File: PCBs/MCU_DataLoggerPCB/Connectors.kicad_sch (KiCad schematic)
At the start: 4 parts, among them J1 Conn_01x04_Pin, J2 Conn_01x04_Pin, J3 Conn_01x09_Pin, J4 Conn_02x03_Odd_Even

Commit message: Project: completed symbol-footprint associations
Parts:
- J1, J2: footprint (none) -> Connector_PinHeader_2.54mm:PinHeader_1x04_P2.54mm_Vertical
- J3: footprint (none) -> Connector_PinHeader_2.54mm:PinHeader_1x09_P2.54mm_Vertical
- J4: footprint (none) -> Connector_PinHeader_2.54mm:PinHeader_2x03_P2.54mm_Vertical
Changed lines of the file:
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@@
 			)
 		)
-		(property "Footprint" ""
+		(property "Footprint" "Connector_PinHeader_2.54mm:PinHeader_2x03_P2.54mm_Vertical"
 			(at 163.83 125.73 0)
 			(effects
@@
 			)
 		)
-		(property "Footprint" ""
+		(property "Footprint" "Connector_PinHeader_2.54mm:PinHeader_1x04_P2.54mm_Vertical"
 			(at 137.16 93.98 0)
 			(effects
@@
 			)
 		)
-		(property "Footprint" ""
+		(property "Footprint" "Connector_PinHeader_2.54mm:PinHeader_1x09_P2.54mm_Vertical"
 			(at 137.16 124.46 0)
 			(effects
@@
 			)
 		)
-		(property "Footprint" ""
+		(property "Footprint" "Connector_PinHeader_2.54mm:PinHeader_1x04_P2.54mm_Vertical"
 			(at 160.02 93.98 0)
 			(effects

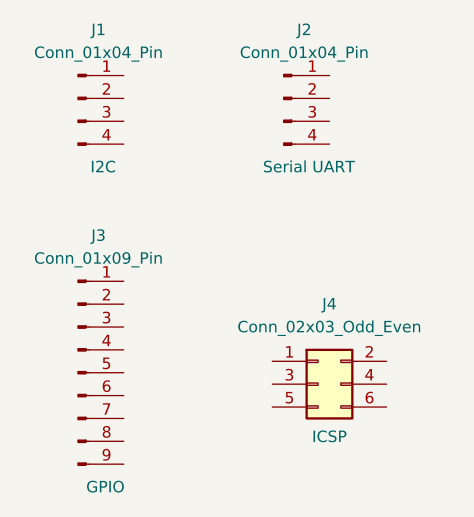
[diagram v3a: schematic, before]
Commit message: Project: completed wiring the second sheet
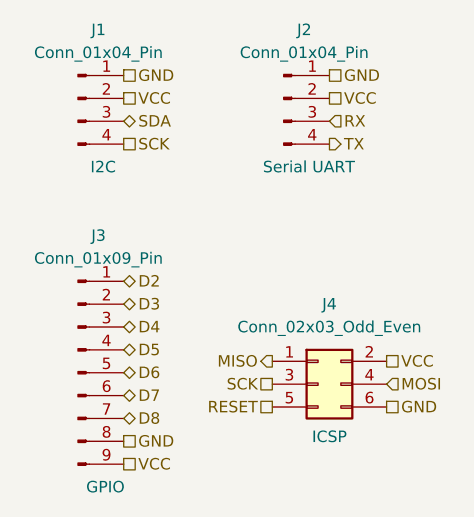
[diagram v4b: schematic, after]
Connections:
- net MISO: now reaches J4.1 (Pin_1)
- net VCC: now reaches J4.2 (Pin_2)
- net VCC: now also J1.2 (Pin_2), J2.2 (Pin_2), J3.9 (Pin_9)
- net SCK: now reaches J4.3 (Pin_3)
- net SCK: now also J1.4 (Pin_4)
- net MOSI: now reaches J4.4 (Pin_4)
- net RESET: now reaches J4.5 (Pin_5)
- net GND: now reaches J4.6 (Pin_6)
- net GND: now also J1.1 (Pin_1), J2.1 (Pin_1), J3.8 (Pin_8)
- net SDA: now reaches J1.3 (Pin_3)
- net D2: now reaches J3.1 (Pin_1)
- net D3: now reaches J3.2 (Pin_2)
- net D4: now reaches J3.3 (Pin_3)
- net D5: now reaches J3.4 (Pin_4)
- net D6: now reaches J3.5 (Pin_5)
- net D7: now reaches J3.6 (Pin_6)
- net D8: now reaches J3.7 (Pin_7)
- net RX: now reaches J2.3 (Pin_3)
- net TX: now reaches J2.4 (Pin_4)
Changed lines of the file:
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@@
 	(generator_version "9.0")
 	(paper "A4")
+	(hierarchical_label "MOSI"
+		(shape input)
+		(at 171.45 125.73 0)
+		(effects
+			(font
+				(size 1.27 1.27)
+			)
+			(justify left)
+		)
+	)
+	(hierarchical_label "D7"
+		(shape bidirectional)
+		(at 142.24 127 0)
+		(effects
+			(font
+				(size 1.27 1.27)
+			)
+			(justify left)
+		)
+	)
+	(hierarchical_label "VCC"
+		(shape passive)
+		(at 142.24 93.98 0)
+		(effects
+			(font
+				(size 1.27 1.27)
+			)
+			(justify left)
+		)
+	)
+	(hierarchical_label "MISO"
+		(shape output)
+		(at 158.75 123.19 180)
+		(effects
+			(font
+				(size 1.27 1.27)
+			)
+			(justify right)
+		)
+	)
+	(hierarchical_label "RX"
+		(shape input)
+		(at 165.1 96.52 0)
+		(effects
+			(font
+				(size 1.27 1.27)
+			)
+			(justify left)
+		)
+	)
+	(hierarchical_label "D5"
+		(shape bidirectional)
+		(at 142.24 121.92 0)
+		(effects
+			(font
+				(size 1.27 1.27)
+			)
+			(justify left)
+		)
+	)
+	(hierarchical_label "D4"
+		(shape bidirectional)
+		(at 142.24 119.38 0)
+		(effects
+			(font
+				(size 1.27 1.27)
+			)
+			(justify left)
+		)
+	)
+	(hierarchical_label "D8"
+		(shape bidirectional)
+		(at 142.24 129.54 0)
+		(effects
+			(font
+				(size 1.27 1.27)
+			)
+			(justify left)
+		)
+	)
+	(hierarchical_label "GND"
+		(shape passive)
+		(at 142.24 132.08 0)
+		(effects
+			(font
+				(size 1.27 1.27)
+			)
+			(justify left)
+		)
+	)
+	(hierarchical_label "D3"
+		(shape bidirectional)
+		(at 142.24 116.84 0)
+		(effects
+			(font
+				(size 1.27 1.27)
+			)
+			(justify left)
+		)
+	)
+	(hierarchical_label "VCC"
+		(shape passive)
+		(at 165.1 93.98 0)
+		(effects
+			(font
+				(size 1.27 1.27)
+			)
+			(justify left)
+		)
+	)
+	(hierarchical_label "SCK"
+		(shape passive)
+		(at 158.75 125.73 180)
+		(effects
+			(font
+				(size 1.27 1.27)
+			)
+			(justify right)
+		)
+	)
+	(hierarchical_label "GND"
+		(shape passive)
+		(at 165.1 91.44 0)
+		(effects
+			(font
+				(size 1.27 1.27)
+			)
+			(justify left)
+		)
+	)
+	(hierarchical_label "VCC"
+		(shape passive)
+		(at 171.45 123.19 0)
+		(effects
+			(font
+				(size 1.27 1.27)
+			)
+			(justify left)
+		)
+	)
+	(hierarchical_label "GND"
+		(shape passive)
+		(at 171.45 128.27 0)
+		(effects
+			(font
+				(size 1.27 1.27)
+			)
+			(justify left)
+		)
+	)
+	(hierarchical_label "GND"
+		(shape passive)
+		(at 142.24 91.44 0)
+		(effects
+			(font
+				(size 1.27 1.27)
+			)
+			(justify left)
+		)
+	)
+	(hierarchical_label "RESET"
+		(shape passive)
+		(at 158.75 128.27 180)
+		(effects
+			(font
+				(size 1.27 1.27)
+			)
+			(justify right)
+		)
+	)
+	(hierarchical_label "VCC"
+		(shape passive)
+		(at 142.24 134.62 0)
+		(effects
+			(font
+				(size 1.27 1.27)
+			)
+			(justify left)
+		)
+	)
+	(hierarchical_label "D6"
+		(shape bidirectional)
+		(at 142.24 124.46 0)
+		(effects
+			(font
+				(size 1.27 1.27)
+			)
+			(justify left)
+		)
+	)
+	(hierarchical_label "SDA"
+		(shape bidirectional)
+		(at 142.24 96.52 0)
+		(effects
+			(font
+				(size 1.27 1.27)
+			)
+			(justify left)
+		)
+	)
+	(hierarchical_label "TX"
+		(shape output)
+		(at 165.1 99.06 0)
+		(effects
+			(font
+				(size 1.27 1.27)
+			)
+			(justify left)
+		)
+	)
+	(hierarchical_label "SCK"
+		(shape passive)
+		(at 142.24 99.06 0)
+		(effects
+			(font
+				(size 1.27 1.27)
+			)
+			(justify left)
+		)
+	)
+	(hierarchical_label "D2"
+		(shape bidirectional)
+		(at 142.24 114.3 0)
+		(effects
+			(font
+				(size 1.27 1.27)
+			)
+			(justify left)
+		)
+	)
 	(symbol
 		(lib_id "Connector_Generic:Conn_02x03_Odd_Even")
